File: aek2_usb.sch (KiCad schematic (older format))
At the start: 237 parts, among them J2 Conn_01x04, J3 Conn_01x04, U1 ATmega32A-PU

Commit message: added firmware
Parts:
- renumbered D11 to D10, D107 to D100, D96 to D101, D101 to D102, D109 to D105, D108 to D106, D87 to D107, D12 to D11, D14 to D12, D15 to D13, D16 to D14, D17 to D15, D18 to D16, D19 to D17, D20 to D18, D21 to D19, D22 to D20, D23 to D21, D24 to D22, D25 to D23, D26 to D24, D27 to D25, D28 to D26, D29 to D27, D30 to D28, D31 to D29, D32 to D30, D33 to D31, D34 to D32, D35 to D33, D36 to D34, D37 to D35, D38 to D36, D39 to D37, D40 to D38, D41 to D39, D5 to D4, D42 to D40, D43 to D41, D44 to D42, D45 to D43, D46 to D44, D47 to D45, D48 to D46, D49 to D47, D50 to D48, D51 to D49, D6 to D5, D52 to D50, D53 to D51, D54 to D52, D55 to D53, D56 to D54, D57 to D55, D58 to D56, D59 to D57, D60 to D58, D61 to D59, D7 to D6, D62 to D60, D63 to D61, D64 to D62, D65 to D63, D66 to D64, D67 to D65, D68 to D66, D69 to D67, D72 to D68, D73 to D69, D8 to D7, D74 to D70, D75 to D71, D78 to D72, D76 to D73, D80 to D74, D79 to D75, D77 to D76, D83 to D77, D84 to D78, D86 to D79, D9 to D8, D92 to D80, D95 to D81, D97 to D82, D98 to D83, D100 to D84, D114 to D85, D90 to D86, D102 to D87, D91 to D88, D111 to D89, D10 to D9, D110 to D90, D105 to D91, D89 to D92, D88 to D93, D93 to D95, D112 to D96, D99 to D97, D106 to D98, D113 to D99, H2 to H1, H1 to H2, J3 to J1, MX12 to MX10, MX99 to MX100, MX107 to MX103, MX106 to MX104, MX85 to MX105, MX13 to MX11, MX14 to MX12, MX15 to MX13, MX16 to MX14, MX17 to MX15, MX18 to MX16, MX19 to MX17, MX20 to MX18, MX21 to MX19, MX3 to MX2, MX22 to MX20, MX23 to MX21, MX24 to MX22, MX25 to MX23, MX26 to MX24, MX27 to MX25, MX28 to MX26, MX29 to MX27, MX30 to MX28, MX31 to MX29, MX4 to MX3, MX32 to MX30, MX33 to MX31, MX34 to MX32, MX35 to MX33, MX36 to MX34, MX37 to MX35, MX38 to MX36, MX39 to MX37, MX40 to MX38, MX41 to MX39, MX5 to MX4, MX42 to MX40, MX43 to MX41, MX44 to MX42, MX45 to MX43, MX46 to MX44, MX47 to MX45, MX48 to MX46, MX49 to MX47, MX50 to MX48, MX51 to MX49, MX6 to MX5, MX52 to MX50, MX53 to MX51, MX54 to MX52, MX55 to MX53, MX56 to MX54, MX57 to MX55, MX58 to MX56, MX59 to MX57, MX60 to MX58, MX61 to MX59, MX7 to MX6, MX62 to MX60, MX63 to MX61, MX64 to MX62, MX65 to MX63, MX66 to MX64, MX67 to MX65, MX70 to MX66, MX71 to MX67, MX72 to MX68, MX73 to MX69, MX8 to MX7, MX76 to MX70, MX74 to MX71, MX78 to MX72, MX77 to MX73, MX75 to MX74, MX81 to MX75, MX82 to MX76, MX84 to MX77, MX90 to MX78, MX93 to MX79, MX9 to MX8, MX95 to MX80, MX96 to MX81, MX98 to MX82, MX112 to MX83, MX88 to MX84, MX100 to MX85, MX89 to MX86, MX109 to MX87, MX108 to MX88, MX103 to MX89, MX10 to MX9, MX87 to MX90, MX86 to MX91, MX91 to MX93, MX110 to MX94, MX97 to MX95, MX104 to MX96, MX111 to MX97, MX105 to MX98, MX94 to MX99
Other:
- moved on the sheet: AVR1, Boot1, C1, C2, C3, C4, C5, D1, D10, D100, D101, D102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

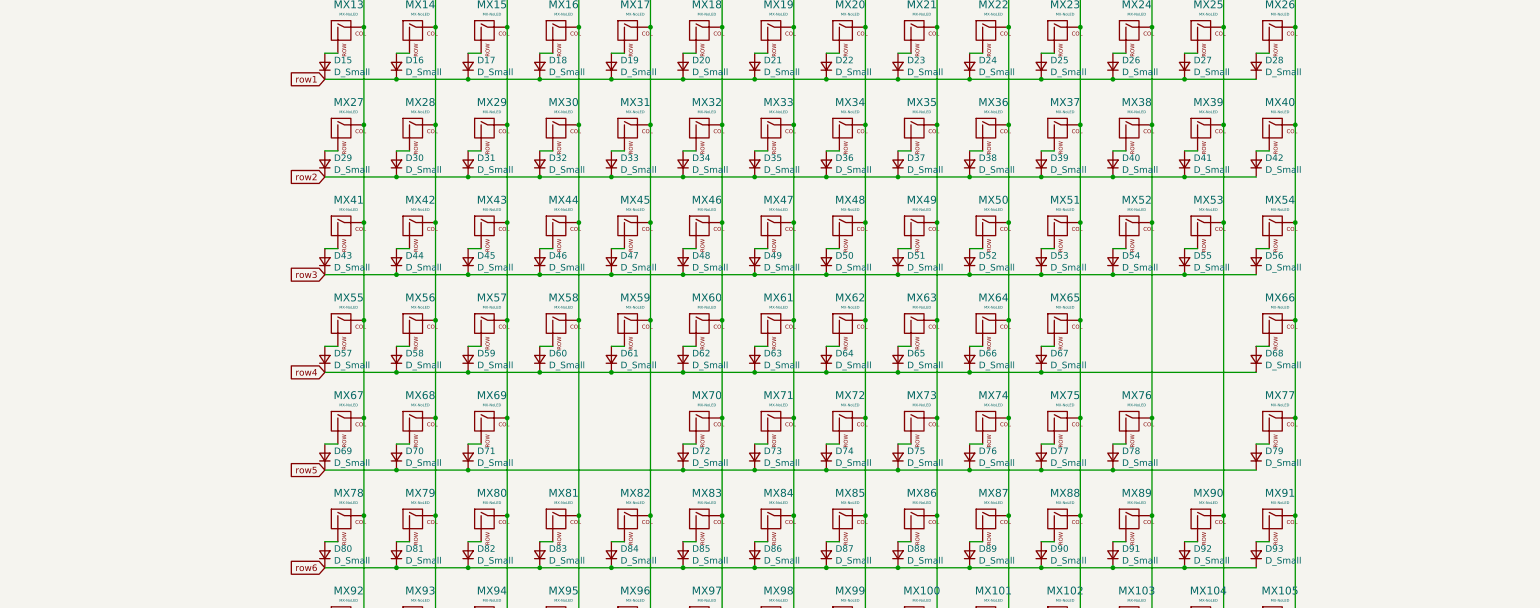
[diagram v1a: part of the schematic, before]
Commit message: added ISO support (UNTESTED!)
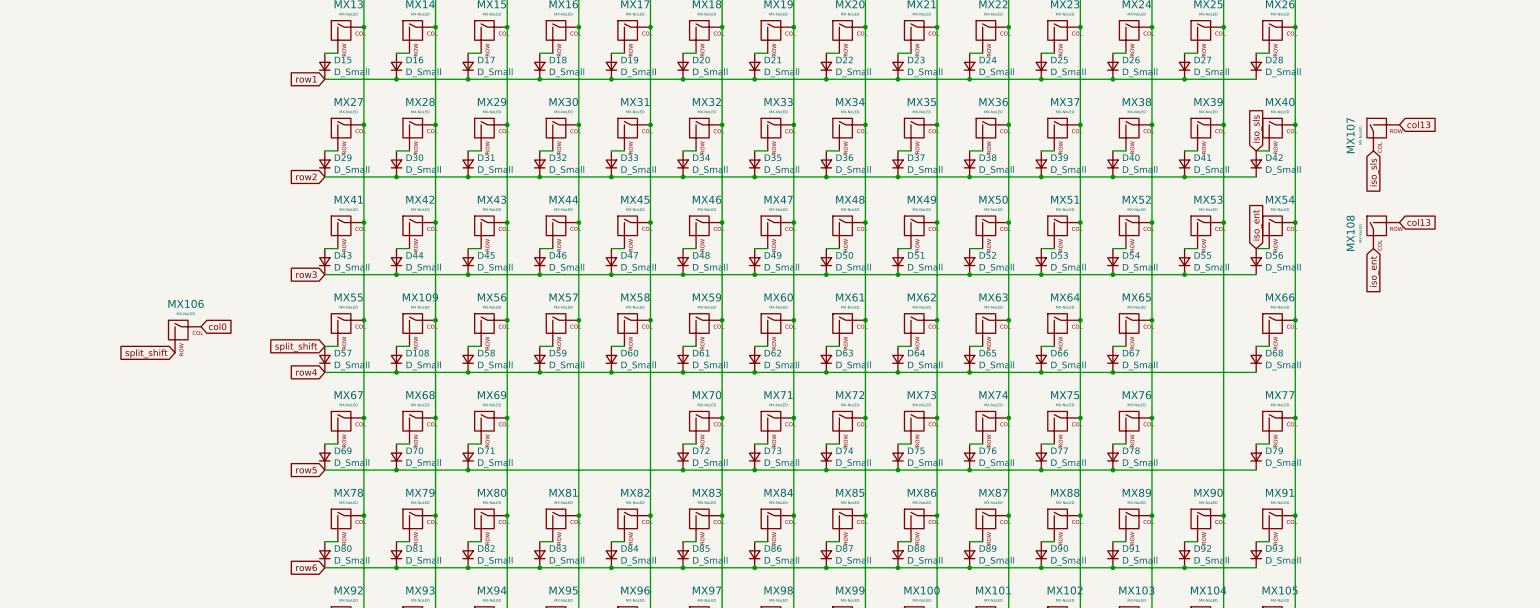
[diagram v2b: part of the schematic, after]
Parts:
- added D108: D_Small, custom_parts:D_DO-35_SOD27_P7.62mm_Horizontal, symbol Device:D_Small
- added MX106: MX-NoLED, Alps_Only:ALPS-1.25U, symbol MX_Alps_Hybrid:MX-NoLED
- added MX107, MX109: MX-NoLED, Alps_Only:ALPS-1U, symbol MX_Alps_Hybrid:MX-NoLED
- added MX108: MX-NoLED, Alps_Only:ALPS-2U, symbol MX_Alps_Hybrid:MX-NoLED
- MX100, MX102, MX26: footprint Alps_Only:ALPS-1U -> Alps_Only:ALPS-2U
- MX27, MX40, MX67, MX69, MX75, MX77: footprint Alps_Only:ALPS-1U -> Alps_Only:ALPS-1.5U
- MX41: footprint Alps_Only:ALPS-1U -> Alps_Only:ALPS-1.75U
- MX54, MX55: footprint Alps_Only:ALPS-1U -> Alps_Only:ALPS-2.25U
- MX66: footprint Alps_Only:ALPS-1U -> Alps_Only:ALPS-2.75U
- MX68, MX76: footprint Alps_Only:ALPS-1U -> Alps_Only:ALPS-1.25U
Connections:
- net col0: now also MX106.1 (COL)
- net col1: now also MX109.1 (COL); no longer MX56.1 (COL)
- net col10: now also MX64.1 (COL); no longer MX65.1 (COL)
- net col11: now also MX65.1 (COL)
- net col13: now also MX107.2 (ROW), MX108.2 (ROW)
- net col2: now also MX56.1 (COL); no longer MX57.1 (COL)
- net col3: now also MX57.1 (COL); no longer MX58.1 (COL)
- net col4: now also MX58.1 (COL); no longer MX59.1 (COL)
- net col5: now also MX59.1 (COL); no longer MX60.1 (COL)
- net col6: now also MX60.1 (COL); no longer MX61.1 (COL)
- net col7: now also MX61.1 (COL); no longer MX62.1 (COL)
- net col8: now also MX62.1 (COL); no longer MX63.1 (COL)
- net col9: now also MX63.1 (COL); no longer MX64.1 (COL)
- net row4: now also D108.1 (K)
- net iso_ent: now reaches D56.2 (A), MX54.2 (ROW)
- net iso_ent: now also MX108.1 (COL)
- net split_shift: now reaches D57.2 (A), MX55.2 (ROW)
- net split_shift: now also MX106.2 (ROW)
- net iso_sls: now reaches D42.2 (A), MX40.2 (ROW)
- net iso_sls: now also MX107.1 (COL)
- new net: D108.2 (A), MX109.2 (ROW)
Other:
- moved on the sheet: D58, D59, D60, D61, D62, D63, D64, D65, D66, D67, MX56, MX57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
